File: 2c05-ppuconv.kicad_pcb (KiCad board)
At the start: 2 copper layers, 13.2 x 9.4 mm, 6 parts, among them J1 Conn_01x03_Male, J2 Conn_01x02_Male, J3 Conn_01x01_Female, U1 74AHCT1G02, U2 74AHCT1G86

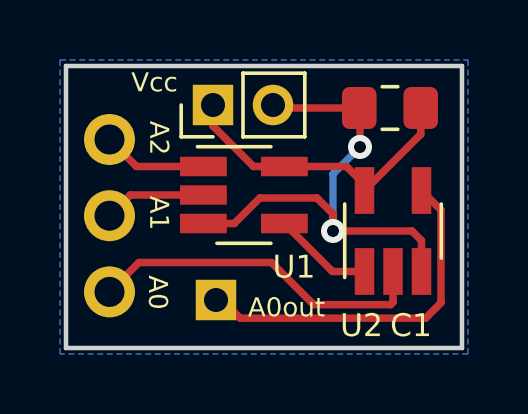
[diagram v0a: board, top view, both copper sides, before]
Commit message: update documentation, swap A0 and out pins on PCB, shrink PCB
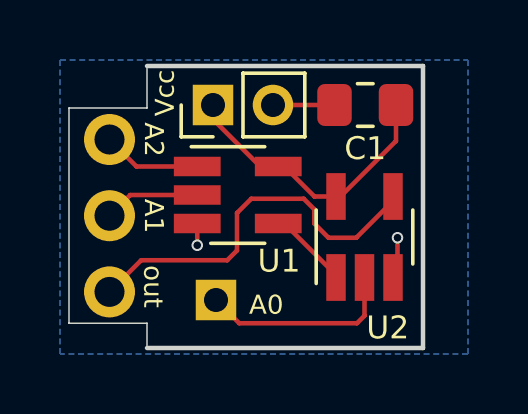
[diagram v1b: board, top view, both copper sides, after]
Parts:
- moved U2 0.97 mm to (128.8, 95.4)
- moved C1 0.83 mm to (128.8, 91.0)
- moved U1 0.20 mm to (124.5, 94.0)
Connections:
- J1 pad 3: /A0 -> /A0out
- J3 pad 1: /A0out -> /A0
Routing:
- net GND: track 17.0 -> 4.10 mm
- net /A0: track 11.5 -> 6.65 mm
- net /A0out: track 12.0 -> 12.9 mm
- net Net-(U1-Pad4): track 3.33 -> 2.62 mm
- net VCC: track 10.3 -> 9.61 mm
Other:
- board size 13.2 x 9.4 mm -> 11.8 x 9.4 mm
- net class Default: clearance 0.2 -> 0.1524; trace_width 0.25 -> 0.1524; via_dia 0.8 -> 0.381; via_drill 0.4 -> 0.254
- rule trace_clearance: 0.2 -> 0.1524
- rule trace_min: 0.2 -> 0.1524
- rule via_min_drill: 0.3 -> 0.254
- rule via_min_size: 0.4 -> 0.381
- board text added: "out"
- board text removed: "A0out"
